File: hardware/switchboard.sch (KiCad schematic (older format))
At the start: 0 parts

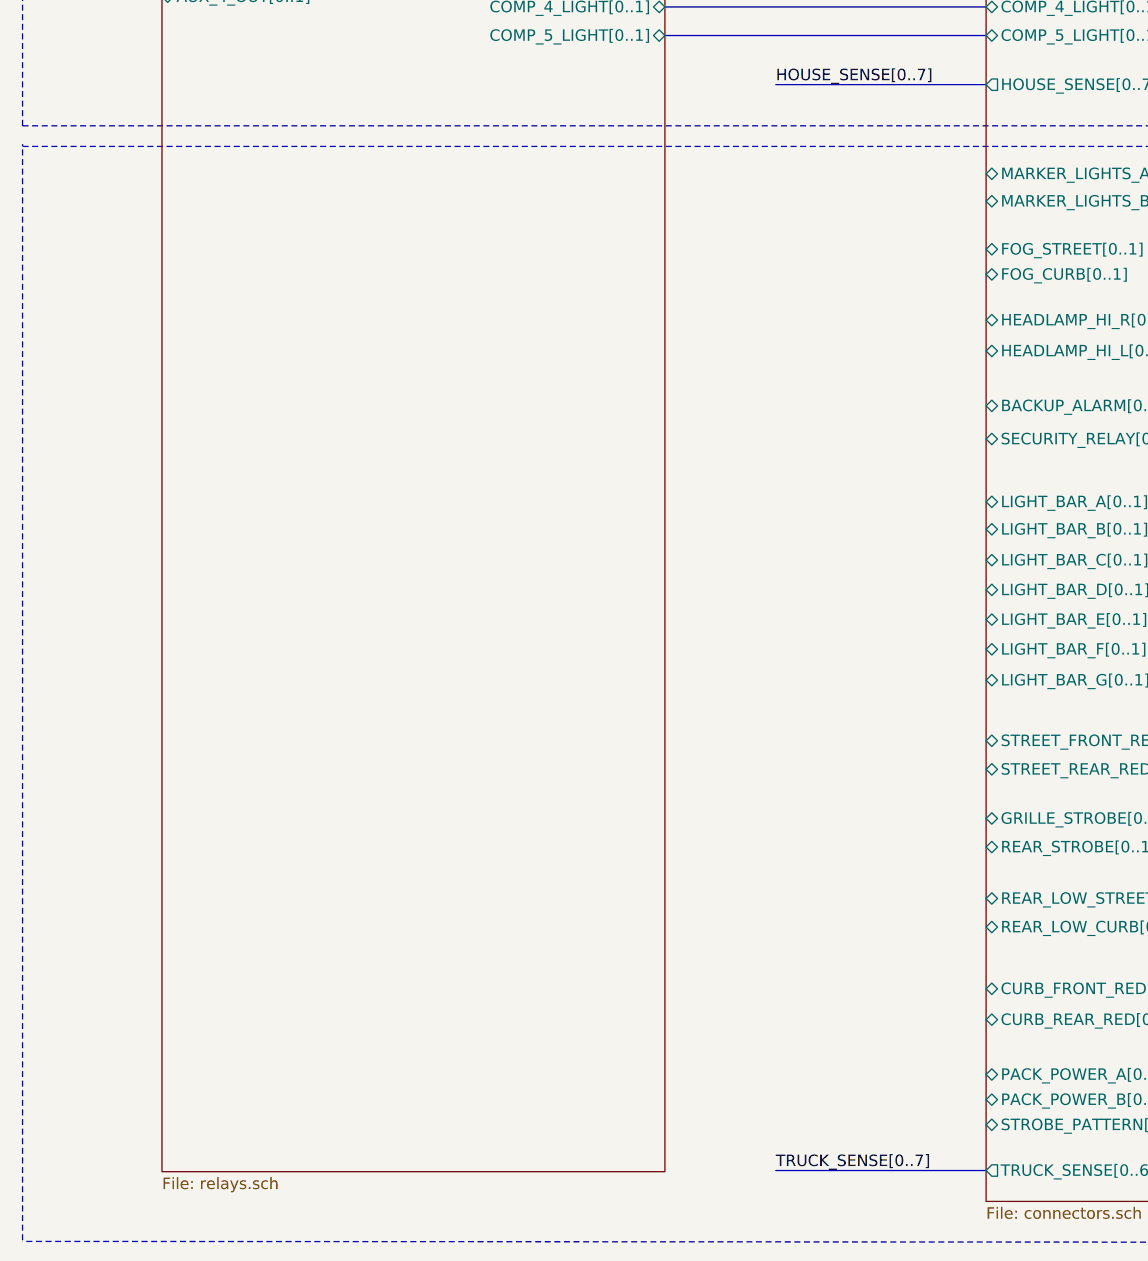
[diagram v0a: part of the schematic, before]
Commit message: hardware: add truck high-side drivers
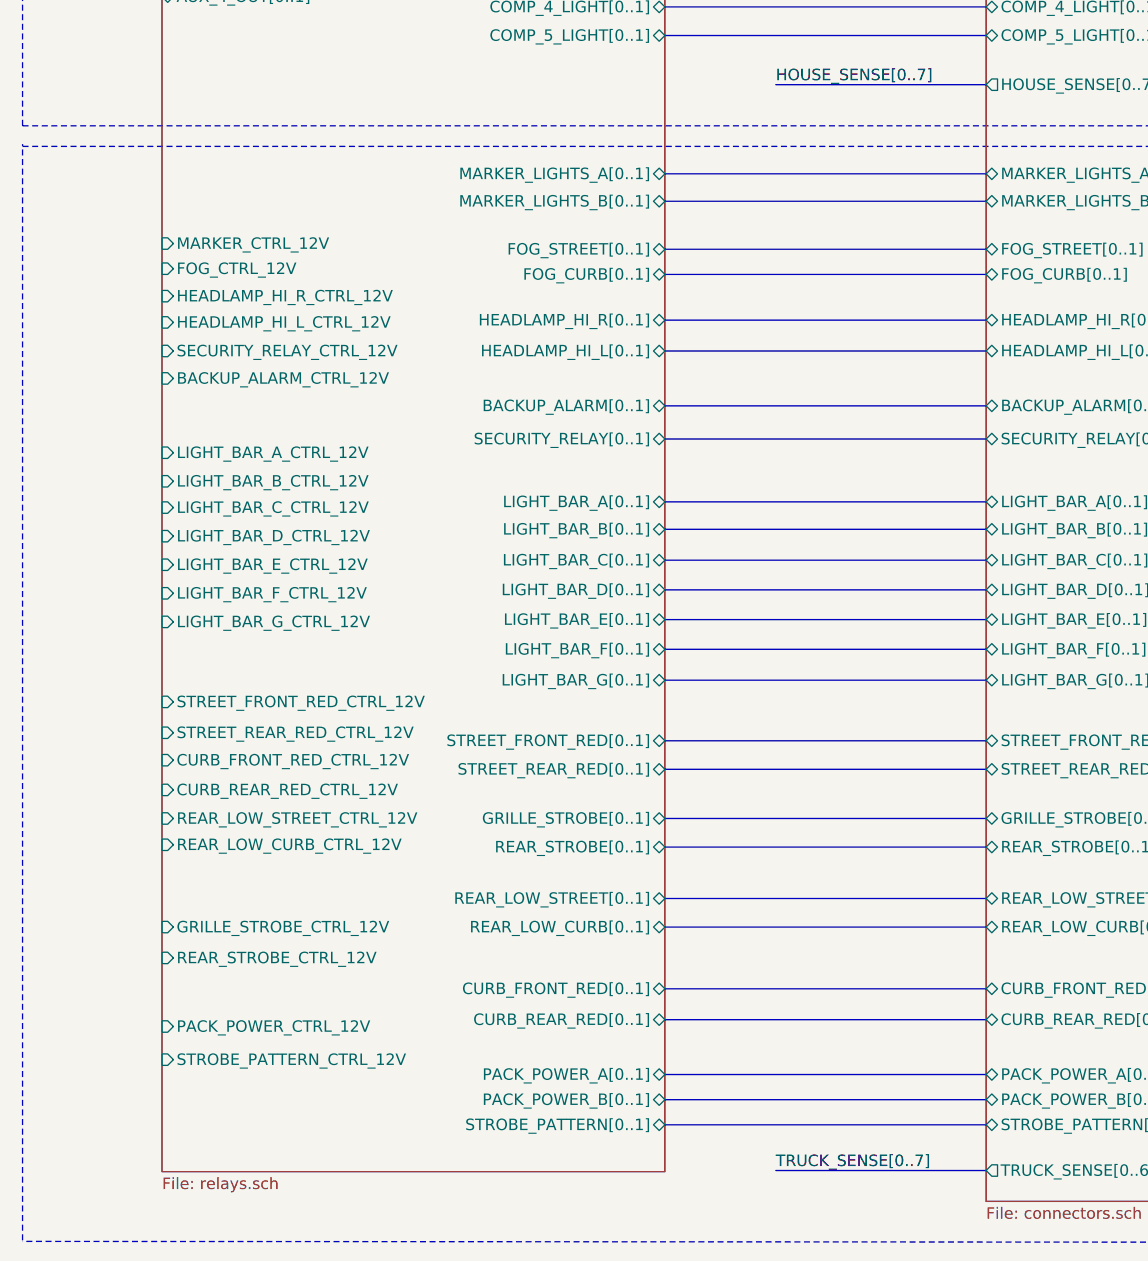
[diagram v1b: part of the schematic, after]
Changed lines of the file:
@@
-$EndSheet
-$Sheet
-S 8820 1190 2200 7935
-U 605C1303
-F0 "Relays" 50
-F1 "relays.sch" 50
-F2 "DRIVER_FLOOD_A[0..1]" B R 11020 1390 50
-F3 "DRIVER_FLOOD_CTRL_12V" I L 8820 1370 50
-F4 "DRIVER_FLOOD_B[0..1]" B R 11020 1510 50
-F5 "PASS_FLOOD_A[0..1]" B R 11020 1690 50
-F6 "PASS_FLOOD_CTRL_12V" I L 8820 1480 50
-F7 "PASS_FLOOD_B[0..1]" B R 11020 1800 50
-F8 "REAR_FLOOD_A[0..1]" B R 11020 1985 50
-F9 "REAR_FLOOD_CTRL_12V" I L 8820 1590 50
-F10 "REAR_FLOOD_B[0..1]" B R 11020 2100 50
-F11 "BENCH_DOME_A[0..1]" B R 11020 2320 50
-F12 "DOME_CTRL_12V" I L 8820 1820 50
-F13 "BENCH_DOME_B[0..1]" B R 11020 2430 50
-F14 "COT_DOME_A[0..1]" B R 11020 2540 50
-F15 "COT_DOME_B[0..1]" B R 11020 2660 50
-F16 "BAR_LIGHT[0..1]" B R 11020 2780 50
-F17 "BAR_LIGHT_CTRL_12V" I L 8820 1925 50
-F18 "STRIP_LIGHT_F[0..1]" B R 11020 2895 50
-F19 "STRIP_LIGHT_CTRL_12V" I L 8820 2020 50
-F20 "STRIP_LIGHT_C[0..1]" B R 11020 3010 50
-F21 "STRIP_LIGHT_R[0..1]" B R 11020 3120 50
-F22 "COMP_1_LIGHT[0..1]" B R 11020 3615 50
-F23 "COMP_1_CTRL_12V" I L 8820 2405 50
-F24 "COMP_2_LIGHT[0..1]" B R 11020 3755 50
-F25 "COMP_2_CTRL_12V" I L 8820 2495 50
-F26 "COMP_3_LIGHT[0..1]" B R 11020 3900 50
-F27 "COMP_3_CTRL_12V" I L 8820 2585 50
-F28 "COMP_4_LIGHT[0..1]" B R 11020 4030 50
-F29 "COMP_4_CTRL_12V" I L 8820 2680 50
-F30 "COMP_5_LIGHT[0..1]" B R 11020 4155 50
-F31 "COMP_5_CTRL_12V" I L 8820 2775 50
-F32 "WATER_PUMP[0..1]" I R 11020 3350 50
-F33 "WATER_PUMP_CTRL_12V" I L 8820 2200 50
-F34 "AUX_1_OUT[0..1]" B L 8820 3600 50
-F35 "AUX_1_CTRL_12V" I L 8820 2955 50
-F36 "AUX_2_OUT[0..1]" B L 8820 3730 50
-F37 "AUX_2_CTRL_12V" I L 8820 3055 50
-F38 "AUX_3_CTRL_12V" I L 8820 3155 50
-F39 "AUX_4_OUT[0..1]" B L 8820 3985 50
-F40 "AUX_4_CTRL_12V" I L 8820 3265 50
-F41 "AUX_3_OUT[0..1]" B L 8820 3860 50
 $EndSheet
 $Sheet
@@
 Wire Notes Line
 	8210 4550 15770 4550
+$Sheet
+S 8820 1190 2200 7935
+U 605C1303
+F0 "Relays" 50
+F1 "relays.sch" 50
+F2 "DRIVER_FLOOD_A[0..1]" B R 11020 1390 50
+F3 "DRIVER_FLOOD_CTRL_12V" I L 8820 1370 50
+F4 "DRIVER_FLOOD_B[0..1]" B R 11020 1510 50
+F5 "PASS_FLOOD_A[0..1]" B R 11020 1690 50
+F6 "PASS_FLOOD_CTRL_12V" I L 8820 1480 50
+F7 "PASS_FLOOD_B[0..1]" B R 11020 1800 50
+F8 "REAR_FLOOD_A[0..1]" B R 11020 1985 50
+F9 "REAR_FLOOD_CTRL_12V" I L 8820 1590 50
+F10 "REAR_FLOOD_B[0..1]" B R 11020 2100 50
+F11 "BENCH_DOME_A[0..1]" B R 11020 2320 50
+F12 "DOME_CTRL_12V" I L 8820 1820 50
+F13 "BENCH_DOME_B[0..1]" B R 11020 2430 50
+F14 "COT_DOME_A[0..1]" B R 11020 2540 50
+F15 "COT_DOME_B[0..1]" B R 11020 2660 50
+F16 "BAR_LIGHT[0..1]" B R 11020 2780 50
+F17 "BAR_LIGHT_CTRL_12V" I L 8820 1925 50
+F18 "STRIP_LIGHT_F[0..1]" B R 11020 2895 50
+F19 "STRIP_LIGHT_CTRL_12V" I L 8820 2020 50
+F20 "STRIP_LIGHT_C[0..1]" B R 11020 3010 50
+F21 "STRIP_LIGHT_R[0..1]" B R 11020 3120 50
+F22 "COMP_1_LIGHT[0..1]" B R 11020 3615 50
+F23 "COMP_1_CTRL_12V" I L 8820 2405 50
+F24 "COMP_2_LIGHT[0..1]" B R 11020 3755 50
+F25 "COMP_2_CTRL_12V" I L 8820 2495 50
+F26 "COMP_3_LIGHT[0..1]" B R 11020 3900 50
+F27 "COMP_3_CTRL_12V" I L 8820 2585 50
+F28 "COMP_4_LIGHT[0..1]" B R 11020 4030 50
+F29 "COMP_4_CTRL_12V" I L 8820 2680 50
+F30 "COMP_5_LIGHT[0..1]" B R 11020 4155 50
+F31 "COMP_5_CTRL_12V" I L 8820 2775 50
+F32 "WATER_PUMP[0..1]" I R 11020 3350 50
+F33 "WATER_PUMP_CTRL_12V" I L 8820 2200 50
+F34 "AUX_1_OUT[0..1]" B L 8820 3600 50
+F35 "AUX_1_CTRL_12V" I L 8820 2955 50
+F36 "AUX_2_OUT[0..1]" B L 8820 3730 50
+F37 "AUX_2_CTRL_12V" I L 8820 3055 50
+F38 "AUX_3_CTRL_12V" I L 8820 3155 50
+F39 "AUX_4_OUT[0..1]" B L 8820 3985 50
+F40 "AUX_4_CTRL_12V" I L 8820 3265 50
+F41 "AUX_3_OUT[0..1]" B L 8820 3860 50
+F42 "FOG_STREET[0..1]" B R 11020 5090 50
+F43 "FOG_CTRL_12V" I L 8820 5175 50
+F44 "HEADLAMP_HI_L[0..1]" B R 11020 5535 50
+F45 "HEADLAMP_HI_L_CTRL_12V" I L 8820 5410 50
+F46 "FOG_CURB[0..1]" B R 11020 5200 50
+F47 "HEADLAMP_HI_R[0..1]" B R 11020 5400 50
+F48 "HEADLAMP_HI_R_CTRL_12V" I L 8820 5295 50
+F49 "BACKUP_ALARM[0..1]" B R 11020 5775 50
+F50 "BACKUP_ALARM_CTRL_12V" I L 8820 5655 50
+F51 "SECURITY_RELAY[0..1]" B R 11020 5920 50
+F52 "SECURITY_RELAY_CTRL_12V" I L 8820 5535 50
+F53 "LIGHT_BAR_A[0..1]" B R 11020 6195 50
+F54 "LIGHT_BAR_A_CTRL_12V" I L 8820 5980 50
+F55 "LIGHT_BAR_B[0..1]" B R 11020 6315 50
+F56 "LIGHT_BAR_B_CTRL_12V" I L 8820 6105 50
+F57 "LIGHT_BAR_C[0..1]" B R 11020 6450 50
+F58 "LIGHT_BAR_C_CTRL_12V" I L 8820 6220 50
+F59 "LIGHT_BAR_D[0..1]" B R 11020 6580 50
+F60 "LIGHT_BAR_D_CTRL_12V" I L 8820 6345 50
+F61 "LIGHT_BAR_E[0..1]" B R 11020 6710 50
+F62 "LIGHT_BAR_E_CTRL_12V" I L 8820 6470 50
+F63 "LIGHT_BAR_F[0..1]" B R 11020 6840 50
+F64 "LIGHT_BAR_F_CTRL_12V" I L 8820 6595 50
+F65 "STREET_FRONT_RED[0..1]" B R 11020 7240 50
+F66 "STREET_FRONT_RED_CTRL_12V" I L 8820 7070 50
+F67 "STREET_REAR_RED[0..1]" B R 11020 7365 50
+F68 "STREET_REAR_RED_CTRL_12V" I L 8820 7205 50
+F69 "GRILLE_STROBE[0..1]" B R 11020 7580 50
+F70 "GRILLE_STROBE_CTRL_12V" I L 8820 8055 50
+F71 "REAR_STROBE[0..1]" B R 11020 7705 50
+F72 "REAR_STROBE_CTRL_12V" I L 8820 8190 50
+F73 "CURB_FRONT_RED[0..1]" B R 11020 8325 50
+F74 "CURB_FRONT_RED_CTRL_12V" I L 8820 7325 50
+F75 "CURB_REAR_RED[0..1]" B R 11020 8460 50
+F76 "CURB_REAR_RED_CTRL_12V" I L 8820 7455 50
+F77 "PACK_POWER_A[0..1]" B R 11020 8700 50
+F78 "PACK_POWER_CTRL_12V" I L 8820 8490 50
+F79 "STROBE_PATTERN[0..1]" B R 11020 8920 50
+F80 "STROBE_PATTERN_CTRL_12V" I L 8820 8635 50
+F81 "MARKER_LIGHTS_A[0..1]" B R 11020 4760 50
+F82 "MARKER_CTRL_12V" I L 8820 5065 50
+F83 "MARKER_LIGHTS_B[0..1]" B R 11020 4880 50
+F84 "PACK_POWER_B[0..1]" B R 11020 8810 50
+F85 "LIGHT_BAR_G[0..1]" B R 11020 6975 50
+F86 "LIGHT_BAR_G_CTRL_12V" I L 8820 6720 50
+F87 "REAR_LOW_STREET[0..1]" B R 11020 7930 50
+F88 "REAR_LOW_STREET_CTRL_12V" I L 8820 7580 50
+F89 "REAR_LOW_CURB[0..1]" B R 11020 8055 50
+F90 "REAR_LOW_CURB_CTRL_12V" I L 8820 7695 50
+$EndSheet
+Wire Bus Line
+	11020 4760 12425 4760
+Wire Bus Line
+	12425 4880 11020 4880
+Wire Bus Line
+	11020 5090 12425 5090
+Wire Bus Line
+	12425 5200 11020 5200
+Wire Bus Line
+	11020 5400 12425 5400
+Wire Bus Line
+	12425 5535 11020 5535
+Wire Bus Line
+	11020 5775 12425 5775
+Wire Bus Line
+	12425 5920 11020 5920
+Wire Bus Line
+	11020 6195 12425 6195
+Wire Bus Line
+	12425 6315 11020 6315
+Wire Bus Line
+	11020 6450 12425 6450
+Wire Bus Line
+	11020 6580 12425 6580
+Wire Bus Line
+	12425 6710 11020 6710
+Wire Bus Line
+	11020 6840 12425 6840
+Wire Bus Line
+	11020 7240 12425 7240
+Wire Bus Line
+	12425 7365 11020 7365
+Wire Bus Line
+	11020 7580 12425 7580
+Wire Bus Line
+	12425 7705 11020 7705
+Wire Bus Line
+	11020 8325 12425 8325
+Wire Bus Line
+	12425 8460 11020 8460
+Wire Bus Line
+	11020 8700 12425 8700
+Wire Bus Line
+	11020 8920 12425 8920
+Wire Bus Line
+	11020 8810 12425 8810
+Wire Bus Line
+	11020 6975 12425 6975
+Wire Bus Line
+	11020 7930 12425 7930
+Wire Bus Line
+	12425 8055 11020 8055
 $EndSCHEMATC
